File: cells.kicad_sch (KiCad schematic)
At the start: 7 parts

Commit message: Layed on board. Still need to route
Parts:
- removed H10, H11, H5, H6, H7, H8, H9: MountingHole_Pad, symbol Mechanical:MountingHole_Pad
- added J5: Conn_01x10_Pin, _BMS:TB4-Hirose, symbol Connector:Conn_01x10_Pin
- added J6: Conn_01x02_Pin, Connector_AMASS:AMASS_XT30PW-M_1x02_P2.50mm_Horizontal, symbol Connector:Conn_01x02_Pin
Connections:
- net CELL1: now also J5.10 (Pin_10)
- net CELL2: now also J5.8 (Pin_8)
- net CELL3: now also J5.6 (Pin_6)
- net CELL4: now also J5.3 (Pin_3)
- net CELL5: now also J5.1 (Pin_1)
- new net BATT+: J6.2 (Pin_2)
- new net BATT-: J6.1 (Pin_1)
- new net NTC1: J5.2 (Pin_2)
- new net NTC2: J5.4 (Pin_4)
- new net NTC3: J5.7 (Pin_7)
- new net NTC4: J5.9 (Pin_9)
- no-connect marks 0 -> 1

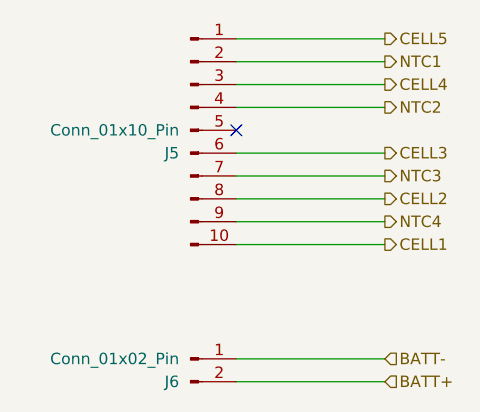
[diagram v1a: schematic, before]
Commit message: Adding proper grounding
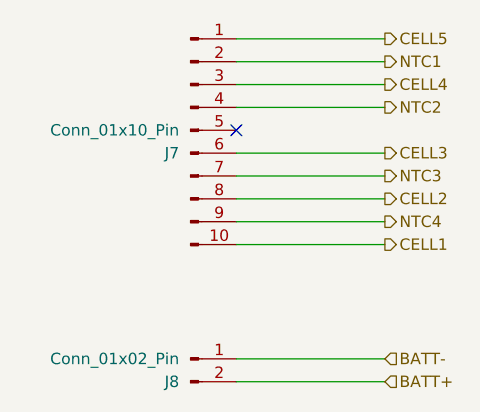
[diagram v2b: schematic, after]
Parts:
- renumbered J5 to J7, J6 to J8
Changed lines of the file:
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@@
 		(on_board yes)
 		(dnp no)
-		(property "Reference" "J5"
+		(property "Reference" "J7"
 			(at 118.11 87.6301 0)
 			(effects
@@
 			(project ""
 				(path "/124184ba-5d68-4d9f-8da6-acc6720ab30b/93f9b420-7cce-46a9-9201-666f07a18f85/72bfe5e0-3464-488b-90f8-8143600a08cb"
-					(reference "J5")
+					(reference "J7")
 					(unit 1)
 				)
@@
 		(on_board yes)
 		(dnp no)
-		(property "Reference" "J6"
+		(property "Reference" "J8"
 			(at 118.11 113.0301 0)
 			(effects
@@
 			(project ""
 				(path "/124184ba-5d68-4d9f-8da6-acc6720ab30b/93f9b420-7cce-46a9-9201-666f07a18f85/72bfe5e0-3464-488b-90f8-8143600a08cb"
-					(reference "J6")
+					(reference "J8")
 					(unit 1)
 				)

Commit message: Lots of changfes
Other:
- company: (none) -> Solar Airplane
- title: (none) -> Cell Inputs
- moved on the sheet: J8
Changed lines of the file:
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@@
 	(generator_version "9.0")
 	(paper "A4")
+	(title_block
+		(title "Cell Inputs")
+		(company "Solar Airplane")
+		(comment 1 "Engineer: Ezzat Suhaime")
+		(comment 2 "Reviwer 1:")
+		(comment 3 "Reviewer 2:")
+	)
 	(no_connect
 		(at 124.46 85.09)
@@
 	(wire
 		(pts
+			(xy 124.46 80.01) (xy 140.97 80.01)
+		)
+		(stroke
+			(width 0)
+			(type default)
+		)
+	)
+	(wire
+		(pts
+			(xy 124.46 109.22) (xy 140.97 109.22)
+		)
+		(stroke
+			(width 0)
+			(type default)
+		)
+	)
+	(wire
+		(pts
 			(xy 124.46 82.55) (xy 140.97 82.55)
 		)
@@
 	(wire
 		(pts
+			(xy 124.46 97.79) (xy 140.97 97.79)
+		)
+		(stroke
+			(width 0)
+			(type default)
+		)
+	)
+	(wire
+		(pts
+			(xy 124.46 74.93) (xy 140.97 74.93)
+		)
+		(stroke
+			(width 0)
+			(type default)
+		)
+	)
+	(wire
+		(pts
+			(xy 124.46 87.63) (xy 140.97 87.63)
+		)
+		(stroke
+			(width 0)
+			(type default)
+		)
+	)
+	(wire
+		(pts
+			(xy 124.46 77.47) (xy 140.97 77.47)
+		)
+		(stroke
+			(width 0)
+			(type default)
+		)
+	)
+	(wire
+		(pts
+			(xy 124.46 106.68) (xy 140.97 106.68)
+		)
+		(stroke
+			(width 0)
+			(type default)
+		)
+	)
+	(wire
+		(pts
+			(xy 124.46 90.17) (xy 140.97 90.17)
+		)
+		(stroke
+			(width 0)
+			(type default)
+		)
+	)
+	(wire
+		(pts
+			(xy 124.46 92.71) (xy 140.97 92.71)
+		)
+		(stroke
+			(width 0)
+			(type default)
+		)
+	)
+	(wire
+		(pts
 			(xy 124.46 95.25) (xy 140.97 95.25)
-		)
-		(stroke
-			(width 0)
-			(type default)
-		)
-	)
-	(wire
-		(pts
-			(xy 124.46 113.03) (xy 140.97 113.03)
-		)
-		(stroke
-			(width 0)
-			(type default)
-		)
-	)
-	(wire
-		(pts
-			(xy 124.46 87.63) (xy 140.97 87.63)
-		)
-		(stroke
-			(width 0)
-			(type default)
-		)
-	)
-	(wire
-		(pts
-			(xy 124.46 92.71) (xy 140.97 92.71)
-		)
-		(stroke
-			(width 0)
-			(type default)
-		)
-	)
-	(wire
-		(pts
-			(xy 124.46 74.93) (xy 140.97 74.93)
-		)
-		(stroke
-			(width 0)
-			(type default)
-		)
-	)
-	(wire
-		(pts
-			(xy 124.46 77.47) (xy 140.97 77.47)
-		)
-		(stroke
-			(width 0)
-			(type default)
-		)
-	)
-	(wire
-		(pts
-			(xy 124.46 110.49) (xy 140.97 110.49)
-		)
-		(stroke
-			(width 0)
-			(type default)
-		)
-	)
-	(wire
-		(pts
-			(xy 124.46 97.79) (xy 140.97 97.79)
-		)
-		(stroke
-			(width 0)
-			(type default)
-		)
-	)
-	(wire
-		(pts
-			(xy 124.46 80.01) (xy 140.97 80.01)
-		)
-		(stroke
-			(width 0)
-			(type default)
-		)
-	)
-	(wire
-		(pts
-			(xy 124.46 90.17) (xy 140.97 90.17)
 		)
 		(stroke
@@
 	(hierarchical_label "BATT-"
 		(shape input)
-		(at 140.97 110.49 0)
+		(at 140.97 106.68 0)
 		(effects
 			(font
@@
 	(hierarchical_label "BATT+"
 		(shape input)
-		(at 140.97 113.03 0)
+		(at 140.97 109.22 0)
 		(effects
 			(font
@@
 	(symbol
 		(lib_id "Connector:Conn_01x02_Pin")
-		(at 119.38 110.49 0)
+		(at 119.38 106.68 0)
 		(unit 1)
 		(exclude_from_sim no)
@@
 		(dnp no)
 		(property "Reference" "J8"
-			(at 118.11 113.0301 0)
+			(at 118.11 109.2201 0)
 			(effects
 				(font
@@
 		)
 		(property "Value" "Conn_01x02_Pin"
-			(at 118.11 110.4901 0)
+			(at 118.11 106.6801 0)
 			(effects
 				(font
@@
 		)
 		(property "Footprint" "Connector_AMASS:AMASS_XT30PW-M_1x02_P2.50mm_Horizontal"
-			(at 119.38 110.49 0)
+			(at 119.38 106.68 0)
 			(effects
 				(font
@@
 		)
 		(property "Datasheet" "~"
-			(at 119.38 110.49 0)
+			(at 119.38 106.68 0)
 			(effects
 				(font
@@
 		)
 		(property "Description" "Generic connector, single row, 01x02, script generated"
-			(at 119.38 110.49 0)
+			(at 119.38 106.68 0)
 			(effects
 				(font
@@
 		)
 		(property "Mfr" ""
-			(at 119.38 110.49 0)
+			(at 119.38 106.68 0)
 			(effects
 				(font
@@
 		)
 		(property "Mfr P/N" ""
-			(at 119.38 110.49 0)
+			(at 119.38 106.68 0)
 			(effects
 				(font
@@
 		)
 		(property "Supplier_1" ""
-			(at 119.38 110.49 0)
+			(at 119.38 106.68 0)
 			(effects
 				(font
@@
 		)
 		(property "Supplier_1 P/N" ""
-			(at 119.38 110.49 0)
+			(at 119.38 106.68 0)
 			(effects
 				(font
@@
 		)
 		(property "Supplier_1 Unit Price" ""
-			(at 119.38 110.49 0)
+			(at 119.38 106.68 0)
 			(effects
 				(font
@@
 		)
 		(property "Supplier_1 Price @ Qty" ""
-			(at 119.38 110.49 0)
+			(at 119.38 106.68 0)
 			(effects
 				(font
@@
 		)
 		(property "Supplier_2" ""
-			(at 119.38 110.49 0)
+			(at 119.38 106.68 0)
 			(effects
 				(font
@@
 		)
 		(property "Supplier_2 P/N" ""
-			(at 119.38 110.49 0)
+			(at 119.38 106.68 0)
 			(effects
 				(font
@@
 		)
 		(property "Supplier_2 Unit Price" ""
-			(at 119.38 110.49 0)
+			(at 119.38 106.68 0)
 			(effects
 				(font
@@
 		)
 		(property "Supplier_2 Price @ Qty" ""
-			(at 119.38 110.49 0)
-			(effects
-				(font
+			(at 119.38 106.68 0)
+			(effects
+				(font

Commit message: Placement
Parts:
- renumbered J7 to J8, J8 to J9
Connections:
- net NTC1 is gone; now on net CELL5: J8.2 (Pin_2)
- net NTC2 is gone; now on net CELL4: J8.4 (Pin_4)
- net NTC3 is gone; now on net CELL2: J8.7 (Pin_7)
- net NTC4 is gone; now on net CELL1: J8.9 (Pin_9)
- net CELL3: now also J8.5 (Pin_5)
- no-connect marks 1 -> 0
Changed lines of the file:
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@@
 		(comment 3 "Reviewer 2:")
 	)
-	(no_connect
-		(at 124.46 85.09)
-	)
-	(wire
-		(pts
-			(xy 124.46 80.01) (xy 140.97 80.01)
+	(junction
+		(at 125.73 97.79)
+		(diameter 0)
+		(color 0 0 0 0)
+	)
+	(junction
+		(at 125.73 87.63)
+		(diameter 0)
+		(color 0 0 0 0)
+	)
+	(junction
+		(at 125.73 80.01)
+		(diameter 0)
+		(color 0 0 0 0)
+	)
+	(junction
+		(at 125.73 74.93)
+		(diameter 0)
+		(color 0 0 0 0)
+	)
+	(junction
+		(at 125.73 92.71)
+		(diameter 0)
+		(color 0 0 0 0)
+	)
+	(wire
+		(pts
+			(xy 125.73 95.25) (xy 125.73 97.79)
+		)
+		(stroke
+			(width 0)
+			(type default)
+		)
+	)
+	(wire
+		(pts
+			(xy 124.46 80.01) (xy 125.73 80.01)
+		)
+		(stroke
+			(width 0)
+			(type default)
+		)
+	)
+	(wire
+		(pts
+			(xy 125.73 90.17) (xy 125.73 92.71)
+		)
+		(stroke
+			(width 0)
+			(type default)
+		)
+	)
+	(wire
+		(pts
+			(xy 124.46 82.55) (xy 125.73 82.55)
+		)
+		(stroke
+			(width 0)
+			(type default)
+		)
+	)
+	(wire
+		(pts
+			(xy 124.46 95.25) (xy 125.73 95.25)
 		)
 		(stroke
@@
 	(wire
 		(pts
-			(xy 124.46 82.55) (xy 140.97 82.55)
-		)
-		(stroke
-			(width 0)
-			(type default)
-		)
-	)
-	(wire
-		(pts
-			(xy 124.46 97.79) (xy 140.97 97.79)
-		)
-		(stroke
-			(width 0)
-			(type default)
-		)
-	)
-	(wire
-		(pts
-			(xy 124.46 74.93) (xy 140.97 74.93)
-		)
-		(stroke
-			(width 0)
-			(type default)
-		)
-	)
-	(wire
-		(pts
-			(xy 124.46 87.63) (xy 140.97 87.63)
-		)
-		(stroke
-			(width 0)
-			(type default)
-		)
-	)
-	(wire
-		(pts
-			(xy 124.46 77.47) (xy 140.97 77.47)
+			(xy 125.73 97.79) (xy 140.97 97.79)
+		)
+		(stroke
+			(width 0)
+			(type default)
+		)
+	)
+	(wire
+		(pts
+			(xy 125.73 74.93) (xy 125.73 77.47)
+		)
+		(stroke
+			(width 0)
+			(type default)
+		)
+	)
+	(wire
+		(pts
+			(xy 124.46 97.79) (xy 125.73 97.79)
+		)
+		(stroke
+			(width 0)
+			(type default)
+		)
+	)
+	(wire
+		(pts
+			(xy 124.46 74.93) (xy 125.73 74.93)
+		)
+		(stroke
+			(width 0)
+			(type default)
+		)
+	)
+	(wire
+		(pts
+			(xy 125.73 87.63) (xy 140.97 87.63)
+		)
+		(stroke
+			(width 0)
+			(type default)
+		)
+	)
+	(wire
+		(pts
+			(xy 125.73 74.93) (xy 140.97 74.93)
+		)
+		(stroke
+			(width 0)
+			(type default)
+		)
+	)
+	(wire
+		(pts
+			(xy 124.46 85.09) (xy 125.73 85.09)
+		)
+		(stroke
+			(width 0)
+			(type default)
+		)
+	)
+	(wire
+		(pts
+			(xy 124.46 87.63) (xy 125.73 87.63)
+		)
+		(stroke
+			(width 0)
+			(type default)
+		)
+	)
+	(wire
+		(pts
+			(xy 125.73 92.71) (xy 140.97 92.71)
+		)
+		(stroke
+			(width 0)
+			(type default)
+		)
+	)
+	(wire
+		(pts
+			(xy 124.46 77.47) (xy 125.73 77.47)
+		)
+		(stroke
+			(width 0)
+			(type default)
+		)
+	)
+	(wire
+		(pts
+			(xy 124.46 90.17) (xy 125.73 90.17)
+		)
+		(stroke
+			(width 0)
+			(type default)
+		)
+	)
+	(wire
+		(pts
+			(xy 125.73 80.01) (xy 125.73 82.55)
 		)
 		(stroke
@@
 	(wire
 		(pts
-			(xy 124.46 90.17) (xy 140.97 90.17)
-		)
-		(stroke
-			(width 0)
-			(type default)
-		)
-	)
-	(wire
-		(pts
-			(xy 124.46 92.71) (xy 140.97 92.71)
-		)
-		(stroke
-			(width 0)
-			(type default)
-		)
-	)
-	(wire
-		(pts
-			(xy 124.46 95.25) (xy 140.97 95.25)
+			(xy 125.73 85.09) (xy 125.73 87.63)
+		)
+		(stroke
+			(width 0)
+			(type default)
+		)
+	)
+	(wire
+		(pts
+			(xy 124.46 92.71) (xy 125.73 92.71)
+		)
+		(stroke
+			(width 0)
+			(type default)
+		)
+	)
+	(wire
+		(pts
+			(xy 125.73 80.01) (xy 140.97 80.01)
 		)
 		(stroke
@@
 		)
 	)
-	(hierarchical_label "NTC2"
-		(shape output)
-		(at 140.97 82.55 0)
-		(effects
-			(font
-				(size 1.27 1.27)
-			)
-			(justify left)
-		)
-	)
-	(hierarchical_label "NTC3"
-		(shape output)
-		(at 140.97 90.17 0)
-		(effects
-			(font
-				(size 1.27 1.27)
-			)
-			(justify left)
-		)
-	)
 	(hierarchical_label "CELL1"
 		(shape output)
@@
 		)
 	)
-	(hierarchical_label "NTC4"
-		(shape output)
-		(at 140.97 95.25 0)
-		(effects
-			(font
-				(size 1.27 1.27)
-			)
-			(justify left)
-		)
-	)
 	(hierarchical_label "CELL2"
 		(shape output)
@@
 		(shape input)
 		(at 140.97 109.22 0)
-		(effects
-			(font
-				(size 1.27 1.27)
-			)
-			(justify left)
-		)
-	)
-	(hierarchical_label "NTC1"
-		(shape output)
-		(at 140.97 77.47 0)
 		(effects
 			(font
@@
 		(on_board yes)
 		(dnp no)
-		(property "Reference" "J7"
+		(property "Reference" "J8"
 			(at 118.11 87.6301 0)
 			(effects
@@
 			(project ""
 				(path "/124184ba-5d68-4d9f-8da6-acc6720ab30b/93f9b420-7cce-46a9-9201-666f07a18f85/72bfe5e0-3464-488b-90f8-8143600a08cb"
-					(reference "J7")
+					(reference "J8")
 					(unit 1)
 				)
@@
 		(on_board yes)
 		(dnp no)
-		(property "Reference" "J8"
+		(property "Reference" "J9"
 			(at 118.11 109.2201 0)
 			(effects
@@
 			(project ""
 				(path "/124184ba-5d68-4d9f-8da6-acc6720ab30b/93f9b420-7cce-46a9-9201-666f07a18f85/72bfe5e0-3464-488b-90f8-8143600a08cb"
-					(reference "J8")
+					(reference "J9")
 					(unit 1)
 				)

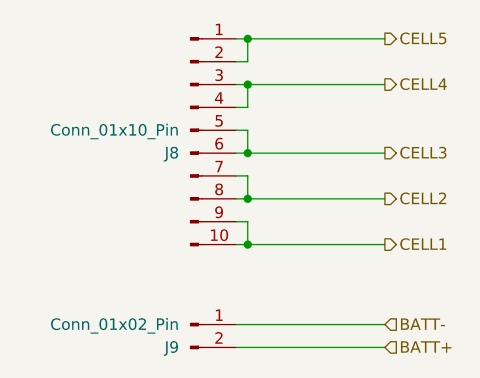
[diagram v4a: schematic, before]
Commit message: Adding in signals and cleaning up schematic
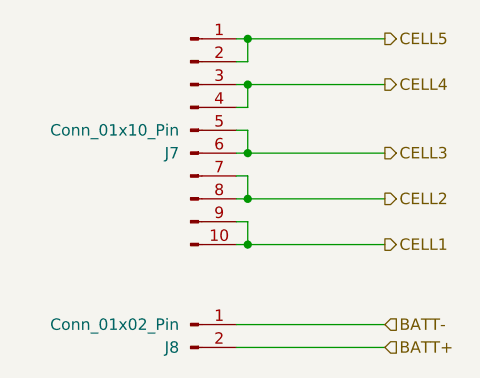
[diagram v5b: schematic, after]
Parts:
- renumbered J8 to J7, J9 to J8
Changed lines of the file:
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@@
 		(on_board yes)
 		(dnp no)
-		(property "Reference" "J8"
+		(property "Reference" "J7"
 			(at 118.11 87.6301 0)
 			(effects
@@
 			(project ""
 				(path "/124184ba-5d68-4d9f-8da6-acc6720ab30b/93f9b420-7cce-46a9-9201-666f07a18f85/72bfe5e0-3464-488b-90f8-8143600a08cb"
-					(reference "J8")
+					(reference "J7")
 					(unit 1)
 				)
@@
 		(on_board yes)
 		(dnp no)
-		(property "Reference" "J9"
+		(property "Reference" "J8"
 			(at 118.11 109.2201 0)
 			(effects
@@
 			(project ""
 				(path "/124184ba-5d68-4d9f-8da6-acc6720ab30b/93f9b420-7cce-46a9-9201-666f07a18f85/72bfe5e0-3464-488b-90f8-8143600a08cb"
-					(reference "J9")
+					(reference "J8")
 					(unit 1)
 				)

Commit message: prepaing for production
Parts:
- J7: now left out of the parts list
- J8: Mfr (none) -> Changzhou Amass Elec; Mfr P/N (none) -> XT30PW-M30.G.Y; Supplier_2 (none) -> JLCPCB; Supplier_2 P/N (none) -> C431092
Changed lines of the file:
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@@
 		(unit 1)
 		(exclude_from_sim no)
-		(in_bom yes)
+		(in_bom no)
 		(on_board yes)
 		(dnp no)
@@
 		)
 		(property "Supplier_2 Price @ Qty" ""
+			(at 119.38 85.09 0)
+			(effects
+				(font
+					(size 1.27 1.27)
+				)
+				(hide yes)
+			)
+		)
+		(property "DigiKey_Part_Number" ""
 			(at 119.38 85.09 0)
 			(effects
@@
 			)
 		)
-		(property "Mfr" ""
-			(at 119.38 106.68 0)
-			(effects
-				(font
-					(size 1.27 1.27)
-				)
-				(hide yes)
-			)
-		)
-		(property "Mfr P/N" ""
+		(property "Mfr" "Changzhou Amass Elec"
+			(at 119.38 106.68 0)
+			(effects
+				(font
+					(size 1.27 1.27)
+				)
+				(hide yes)
+			)
+		)
+		(property "Mfr P/N" "XT30PW-M30.G.Y"
 			(at 119.38 106.68 0)
 			(effects
@@
 			)
 		)
-		(property "Supplier_2" ""
-			(at 119.38 106.68 0)
-			(effects
-				(font
-					(size 1.27 1.27)
-				)
-				(hide yes)
-			)
-		)
-		(property "Supplier_2 P/N" ""
+		(property "Supplier_2" "JLCPCB"
+			(at 119.38 106.68 0)
+			(effects
+				(font
+					(size 1.27 1.27)
+				)
+				(hide yes)
+			)
+		)
+		(property "Supplier_2 P/N" "C431092"
 			(at 119.38 106.68 0)
 			(effects
@@
 			(at 119.38 106.68 0)
 			(effects
+				(font
+					(size 1.27 1.27)
+				)
+				(hide yes)
+			)
+		)
+		(property "DigiKey_Part_Number" ""
+			(at 119.38 106.68 0)
+			(effects
